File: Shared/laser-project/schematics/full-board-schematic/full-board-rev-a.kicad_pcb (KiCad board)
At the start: 2 copper layers, 109.2 x 40.6 mm, 44 parts, among them CON1 USB-B, SW1 PUSHSWITCH, T1 OP598C, T2 BSS138, T3 BSS138, U1 AT90USB1286, U2 DS1077, U3 AD8302, U4 MCP1825, U5 MCP1825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

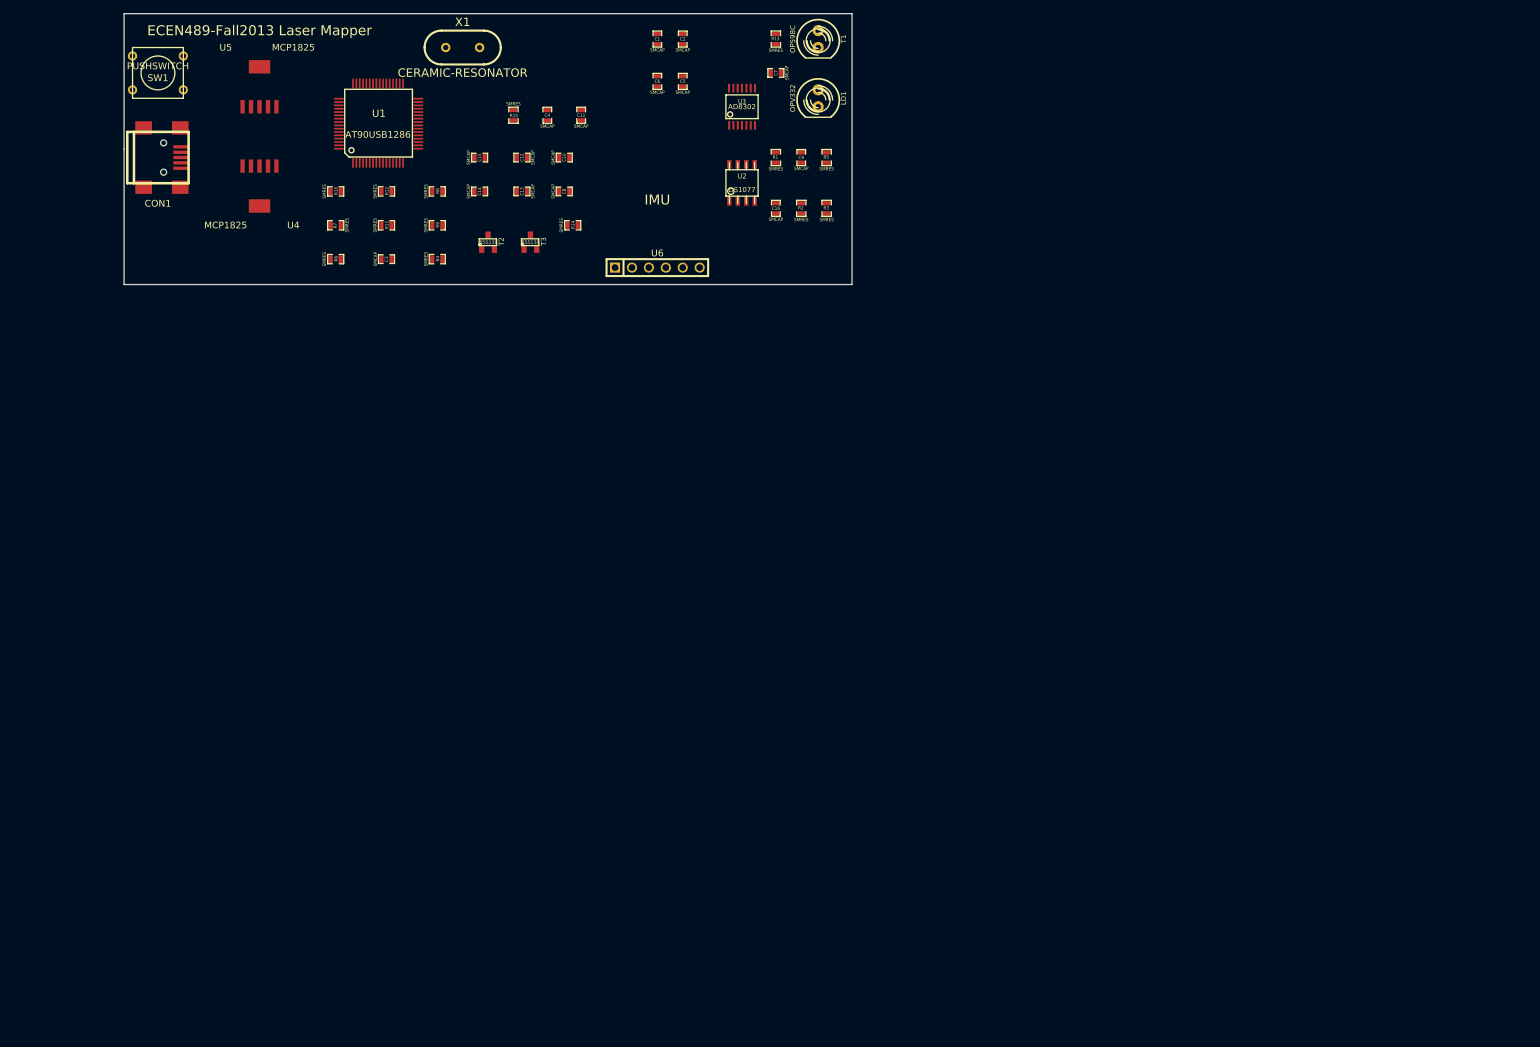
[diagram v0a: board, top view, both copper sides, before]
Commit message: 
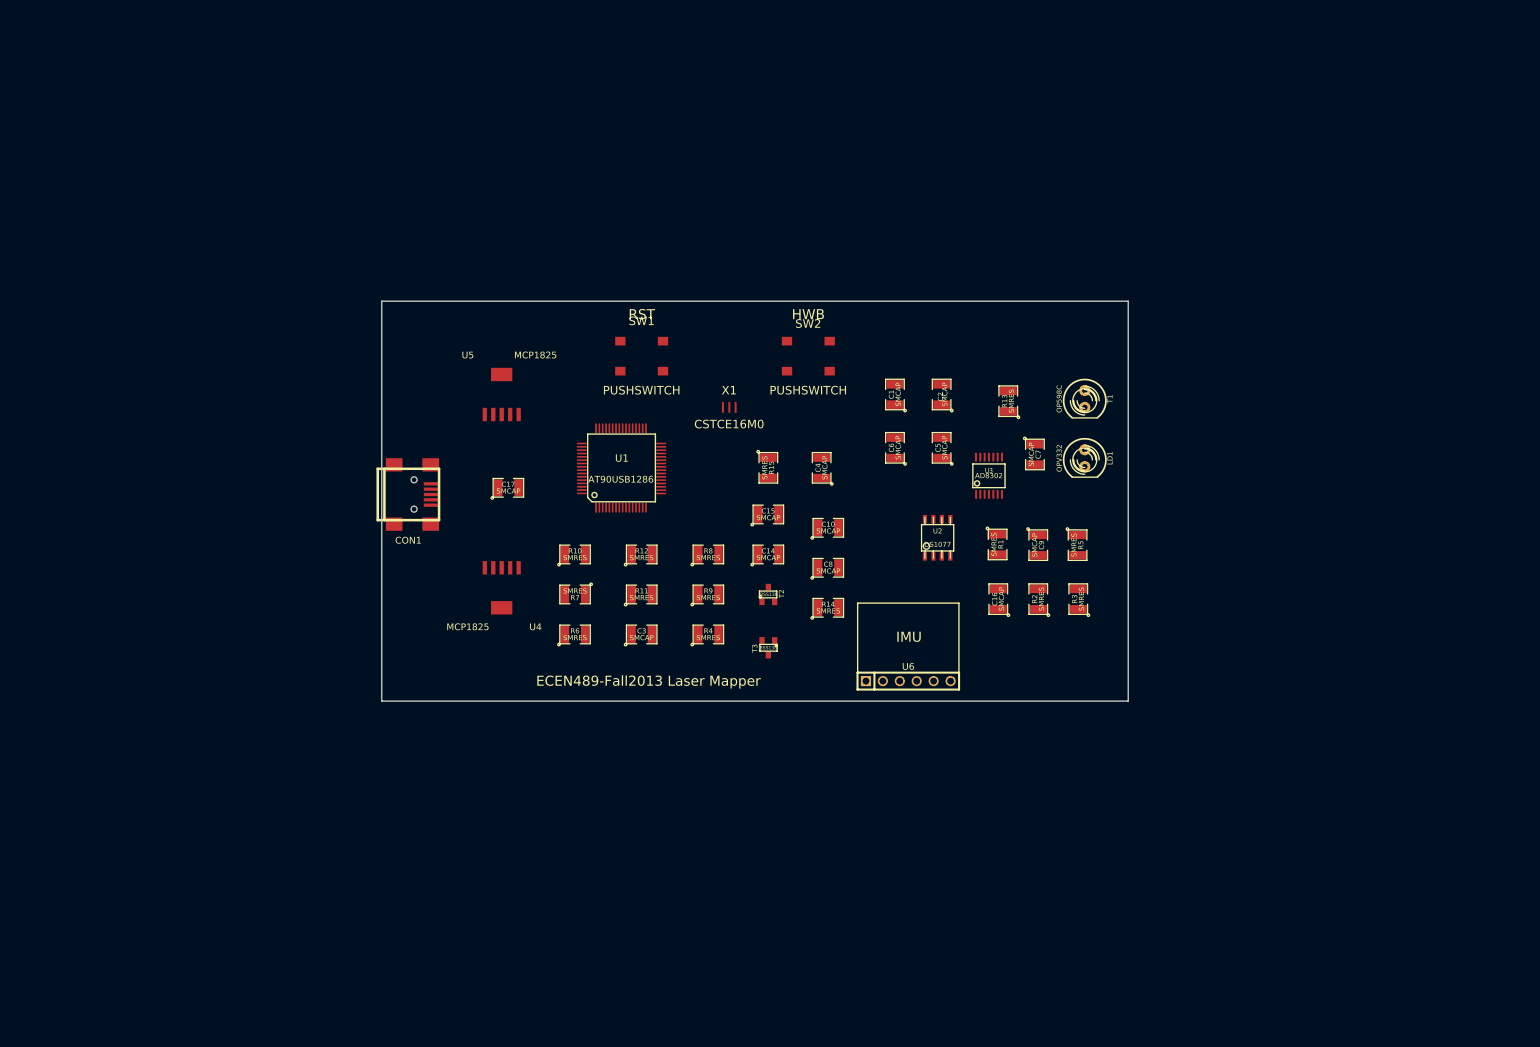
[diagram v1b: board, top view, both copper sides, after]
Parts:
- removed C11, C12, C13: SMCAP, SM0603_Capa
- added C17: SMCAP, SM1210, F.Cu at (111.0, 94.0)
- added SW2: PUSHSWITCH, SW, F.Cu at (156.0, 72.0)
- C1, C10, C14, C15, C16, C2, C3, C4, C5, C6, C7, C8, C9: footprint SM0603_Capa -> SM1210
- CON1: value USB-B -> USB-MINI-B
- R1, R10, R11, R12, R13, R14, R15, R2, R3, R4, R5, R6, R7, R8, R9: footprint SM0603_Resistor -> SM1210
- SW1: footprint SW_PUSH_SMALL -> SW
- X1: value CERAMIC-RESONATOR -> CSTCE16M0; footprint HC-49V -> 16MHzRES
- moved SW1 83.0 mm to (131.0, 72.0)
- moved U6 72.6 mm to (171.0, 123.0)
- moved T3 70.5 mm to (150.0, 118.0), turned to 180 degrees
- moved U4 70.4 mm to (110.0, 106.0)
- moved R3 69.7 mm to (196.5, 110.7)
- moved C14 69.6 mm to (150.0, 104.0)
- moved R4 69.5 mm to (141.0, 116.0)
- moved R5 69.3 mm to (196.4, 102.6), turned to 270 degrees
- moved C7 69.2 mm to (190.0, 89.0), turned to 270 degrees
- moved R14 69.0 mm to (159.0, 112.0)
- moved C8 69.0 mm to (159.0, 106.0)
- moved C15 68.9 mm to (150.0, 98.0)
- moved R9 68.7 mm to (141.0, 110.0)
- moved R2 68.6 mm to (190.5, 110.7)
- moved C10 68.2 mm to (159.0, 100.0)
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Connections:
- CON1 pad 4: GND -> (no net)
- CON1 pad 5: (no net) -> GND
- R10 pad 2: N-000009 -> /regulator_3.3V
- R6 pad 2: N-0000015 -> (no net)
- U1 pad 1: /E6 -> (no net)
- U1 pad 10: /B0 -> (no net)
- U1 pad 11: /B1 -> (no net)
- U1 pad 12: /B2 -> (no net)
- U1 pad 13: /B3 -> (no net)
- U1 pad 14: /B4 -> (no net)
- U1 pad 15: /B5 -> (no net)
- U1 pad 16: /B6 -> (no net)
- U1 pad 17: /B7 -> (no net)
- U1 pad 18: /E4 -> (no net)
- U1 pad 19: /E5 -> (no net)
- U1 pad 2: /E7 -> (no net)
- U1 pad 21: N-0000073 -> /regulator_5V
- U1 pad 27: /D2 -> (no net)
- U1 pad 28: /D3 -> (no net)
- U1 pad 29: /D4 -> (no net)
- U1 pad 30: /D5 -> (no net)
- U1 pad 31: /D6 -> (no net)
- U1 pad 32: /D7 -> (no net)
- U1 pad 33: /E0 -> (no net)
- U1 pad 34: /E1 -> (no net)
- U1 pad 37: /C2 -> (no net)
- U1 pad 38: /C3 -> (no net)
- U1 pad 39: /C4 -> (no net)
- U1 pad 40: /C5 -> (no net)
- U1 pad 41: /C6 -> (no net)
- U1 pad 42: /C7 -> (no net)
- U1 pad 43: N-0000069 -> /hwb_sig
- U1 pad 44: /A7 -> (no net)
- U1 pad 45: /A6 -> (no net)
- U1 pad 46: /A5 -> (no net)
- U1 pad 47: /A4 -> (no net)
- U1 pad 48: /A3 -> (no net)
- U1 pad 49: /A2 -> (no net)
- U1 pad 50: /A1 -> (no net)
- U1 pad 51: /A0 -> (no net)
- U1 pad 52: N-0000068 -> /regulator_5V
- U1 pad 54: /F7 -> (no net)
- U1 pad 55: /F6 -> (no net)
- U1 pad 56: /F5 -> (no net)
- U1 pad 57: /F4 -> (no net)
- U1 pad 58: /F3 -> (no net)
- U1 pad 59: /F2 -> (no net)
- U1 pad 64: N-0000074 -> /regulator_5V
- U1 pad 9: N-0000071 -> (no net)
- U2 pad 2: N-0000064 -> (no net)
- U6 pad 1: N-0000046 -> (no net)
- U6 pad 2: N-0000047 -> (no net)
- X1 pad 1: /xtal1_sig -> /xtal2_sig
- X1 pad 2: /xtal2_sig -> GND
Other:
- board size 109.2 x 40.6 mm -> 112 x 60 mm
- net class Default: clearance 0.01 -> 0.5
- rule trace_clearance: 0.01 -> 0.5
- board text added: "HWB"
- board text added: "RST"

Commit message: Had forgotten to replace some labels.
While debugging, I had moved some regulator_5V labels to see if they
were causing a problem.  They weren't, but I forgot to move them back.
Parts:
- CON1: footprint USB_MINI_B -> usb-mini-b
- moved R9 37.6 mm to (105.7, 97.3)
- moved R8 36.9 mm to (105.7, 93.2)
- moved C17 17.9 mm to (101.1, 109.0)
- moved U1 3.47 mm to (125.0, 93.0), turned to 270 degrees
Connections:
- R6 pad 2: (no net) -> /regulator_5V
- U3 pad 4: /regulator_5V -> /ad8302_vpos

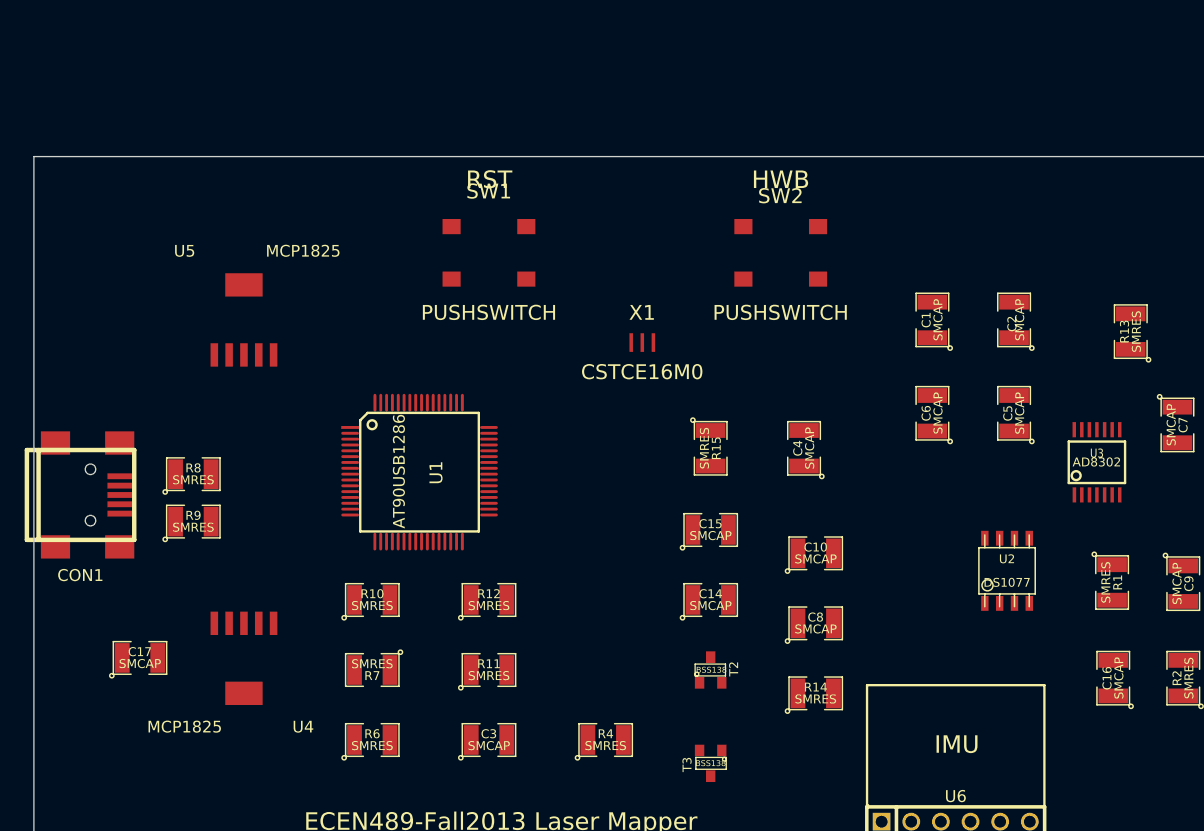
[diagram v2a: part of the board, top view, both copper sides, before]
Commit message: Routing progress.
Have routed the two power supplies and their supporting circuitry.
Each of these modules only requires the front side of the board.
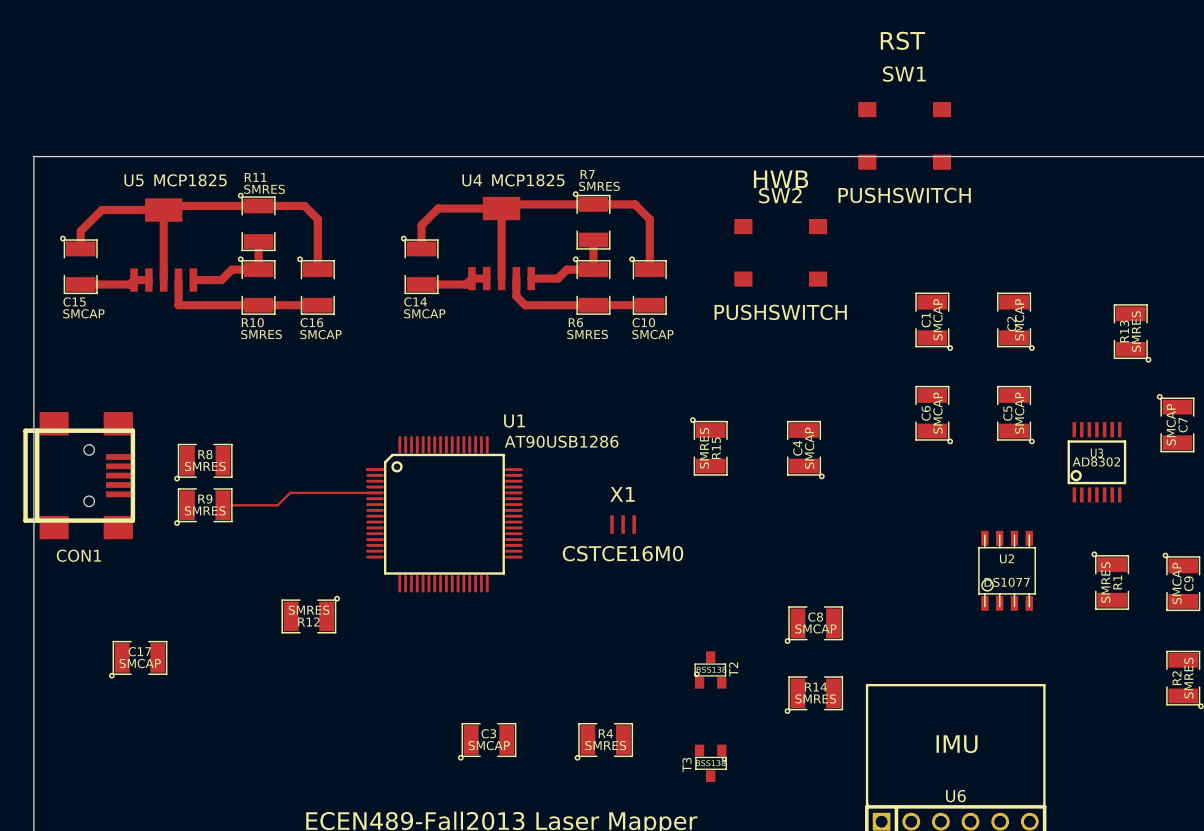
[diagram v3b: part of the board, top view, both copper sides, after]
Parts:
- moved C16 75.9 mm to (116.3, 77.2), turned to 270 degrees
- moved C15 58.5 mm to (96.0, 75.4), turned to 270 degrees
- moved R6 43.2 mm to (140.0, 77.2), turned to 270 degrees
- moved R11 43.0 mm to (111.3, 71.8), turned to 270 degrees
- moved R7 42.8 mm to (140.0, 71.6), turned to 270 degrees
- moved C14 37.8 mm to (125.2, 75.4), turned to 270 degrees
- moved SW1 37.0 mm to (166.6, 62.0)
- moved U4 36.9 mm to (132.1, 76.5), turned to 0 degrees
- moved R10 28.5 mm to (111.3, 77.2), turned to 270 degrees
- moved C10 26.9 mm to (144.8, 77.2), turned to 270 degrees
- moved X1 15.7 mm to (142.5, 97.5)
- moved R12 15.5 mm to (115.6, 105.4), turned to 180 degrees
- moved U5 9.41 mm to (103.1, 76.6)
- moved U1 4.19 mm to (127.1, 96.6)
- moved R9 1.73 mm to (106.7, 95.9)
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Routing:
- net GND: track 0.00 -> 66.7 mm
- net /regulator_3.3V: track 0.00 -> 14.1 mm
- net N-000002: track 0.00 -> 13.5 mm
- net /regulator_5V: track 0.00 -> 13.3 mm
- net /usb_5V: track 0.00 -> 11.8 mm
- net N-000006: track 0.00 -> 8.37 mm
- net N-000004: track 0.00 -> 8.19 mm
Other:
- net class Default: clearance 0.5 -> 0.2; trace_width 0.254 -> 0.2
- rule trace_clearance: 0.5 -> 0.2
- rule trace_min: 0.254 -> 0.2

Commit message: Continued routing work.
I still need to add some encoder interface pins.
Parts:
- added CON2: JTAG-10MIL-HDR, JTAG-10mil-hdr, F.Cu at (194.6, 122.2)
- moved C3 79.4 mm to (210.1, 109.0)
- moved R4 70.8 mm to (209.3, 97.3)
- moved C8 69.4 mm to (228.3, 107.7)
- moved C6 61.1 mm to (228.3, 102.6), turned to 0 degrees
- moved U3 56.8 mm to (238.5, 104.9), turned to 270 degrees
- moved C5 53.3 mm to (228.3, 98.0), turned to 0 degrees
- moved C7 44.9 mm to (228.3, 112.3), turned to 0 degrees
- moved R2 34.4 mm to (223.3, 100.3)
- moved R3 26.8 mm to (223.3, 110.0), turned to 270 degrees
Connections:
- U1 pad 54: (no net) -> /jtag_tdi
- U1 pad 55: (no net) -> /jtag_tdo
- U1 pad 56: (no net) -> /jtag_tms
- U1 pad 57: (no net) -> /jtag_tck
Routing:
- net /ad8302_inpb: track 0.00 -> 9.10 mm
- net /ad8302_inpa: track 0.00 -> 8.59 mm
- net GND: track 66.7 -> 74.4 mm
- net /ad8302_ofsb: track 0.00 -> 6.87 mm
- net /ad8302_ofsa: track 0.00 -> 6.53 mm
